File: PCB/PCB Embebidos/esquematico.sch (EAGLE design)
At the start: 27 parts, among them IC1 LM358N, IC2 317T, T1 BT138-V

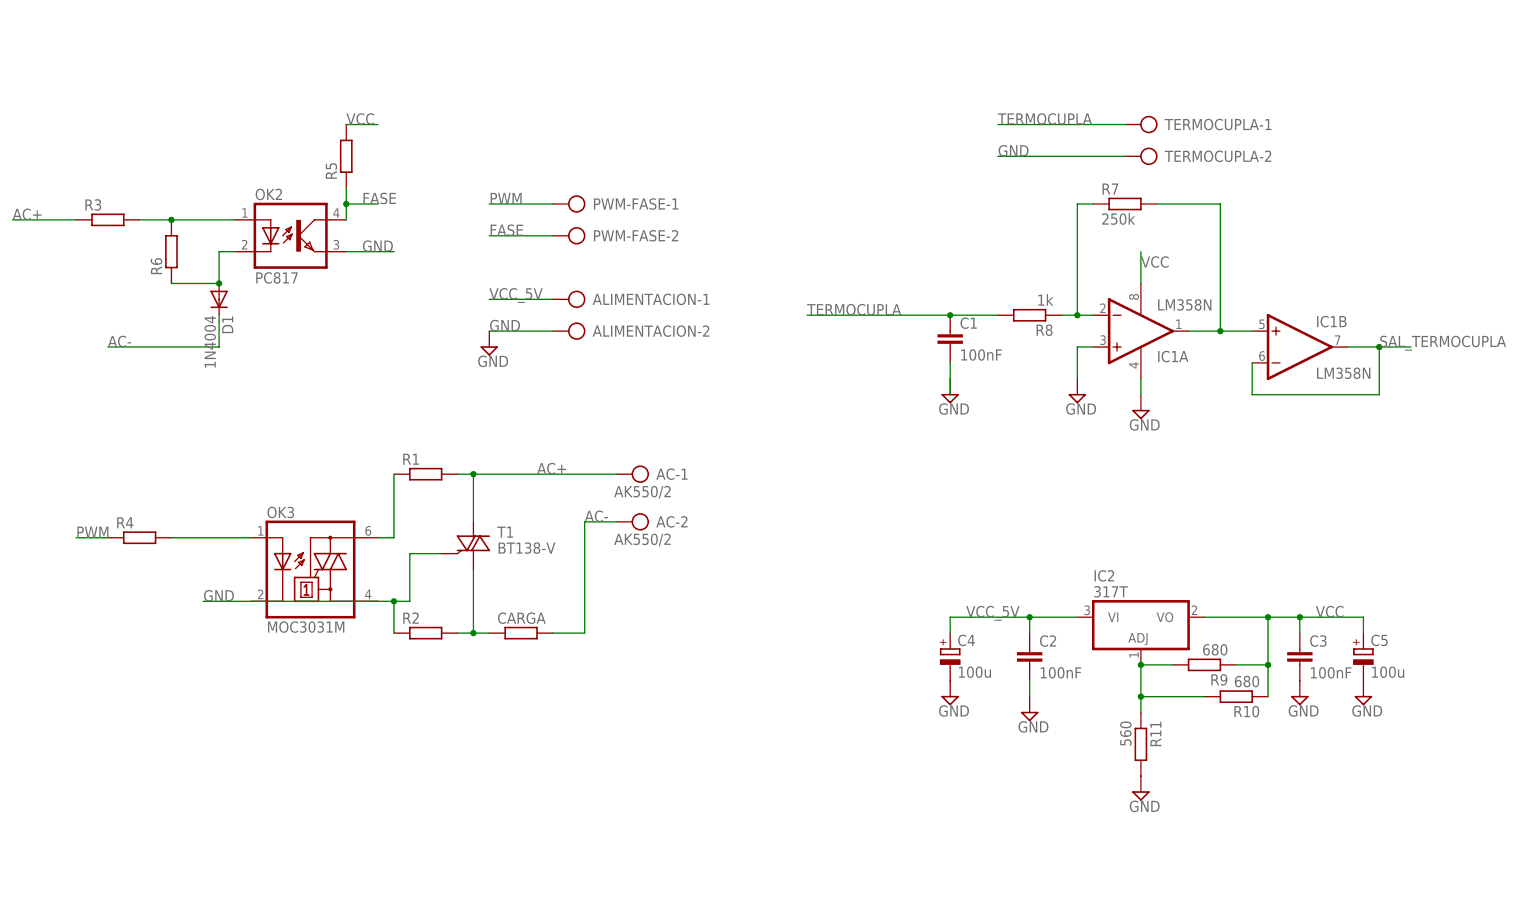
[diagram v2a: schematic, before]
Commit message: Cambie las resistencias del PCB a smd. Tambien modifique las borneras para usar unas de 5mm
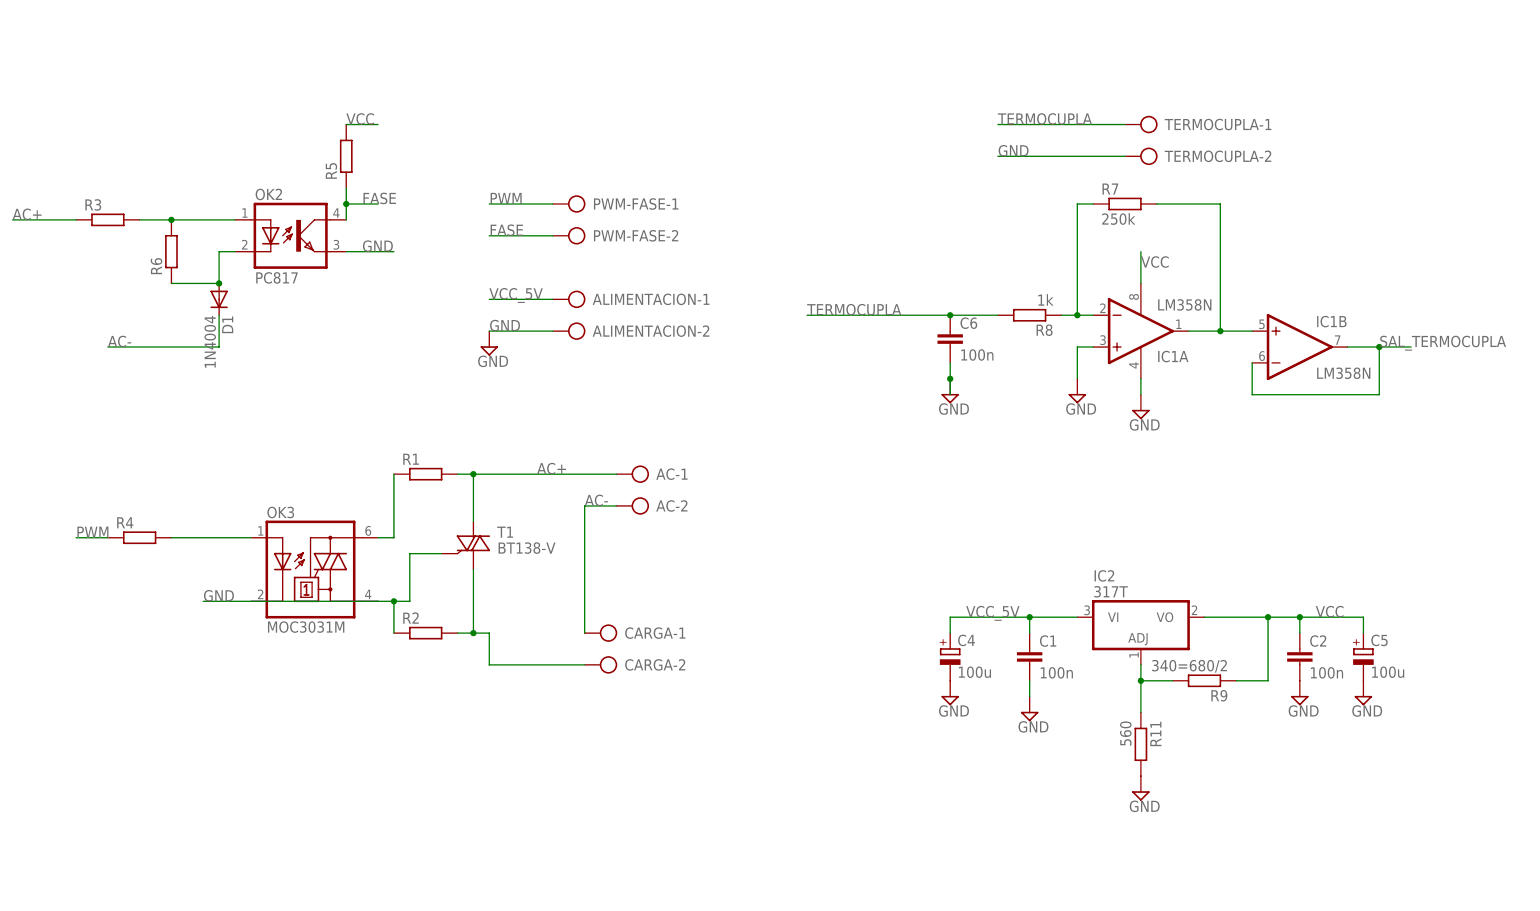
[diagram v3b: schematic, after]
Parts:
- removed C3: 100nF, capacitor-wima:C2,5-3
- removed R10: 680, resistor:R-EU_0207/10
- added C6: 100n, eagle-ltspice:CC1206
- AC: value AK550/2 -> (none); device con-ptr500:AK550/2 -> con-ptr500:AK300/2
- C1, C2: value 100nF -> 100n; device capacitor-wima:C2,5-3 -> eagle-ltspice:CC1206
- CARGA: device resistor:R-EU_0207/10 -> con-ptr500:AK300/2
- R1, R11, R2, R4, R5, R6, R7, R8: device resistor:R-EU_0207/10 -> resistor:R-EU_R1206
- R9: value 680 -> 340=680/2; device resistor:R-EU_0207/10 -> resistor:R-EU_R1206
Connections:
- net AC-: now also CARGA-1.KL; no longer AC-2.KL, CARGA.2
- net GND: now also C6.2; no longer C3.2
- net N$4: now also CARGA-2.KL; no longer CARGA.1
- net N$6: no longer R10.2
- net TERMOCUPLA: now also C6.1; no longer C1.1
- net VCC: now also C2.1; no longer C3.1, R10.1
- net VCC_5V: now also C1.1; no longer C2.1
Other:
- moved on the sheet: AC-2, C1, C2, R9

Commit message: Agregue los valores de algunas resistencias que me faltaban, agregue el pt100, y agregue un pdf con una foto del esquematico para poder revisarlo mas facil sin abrir eagle
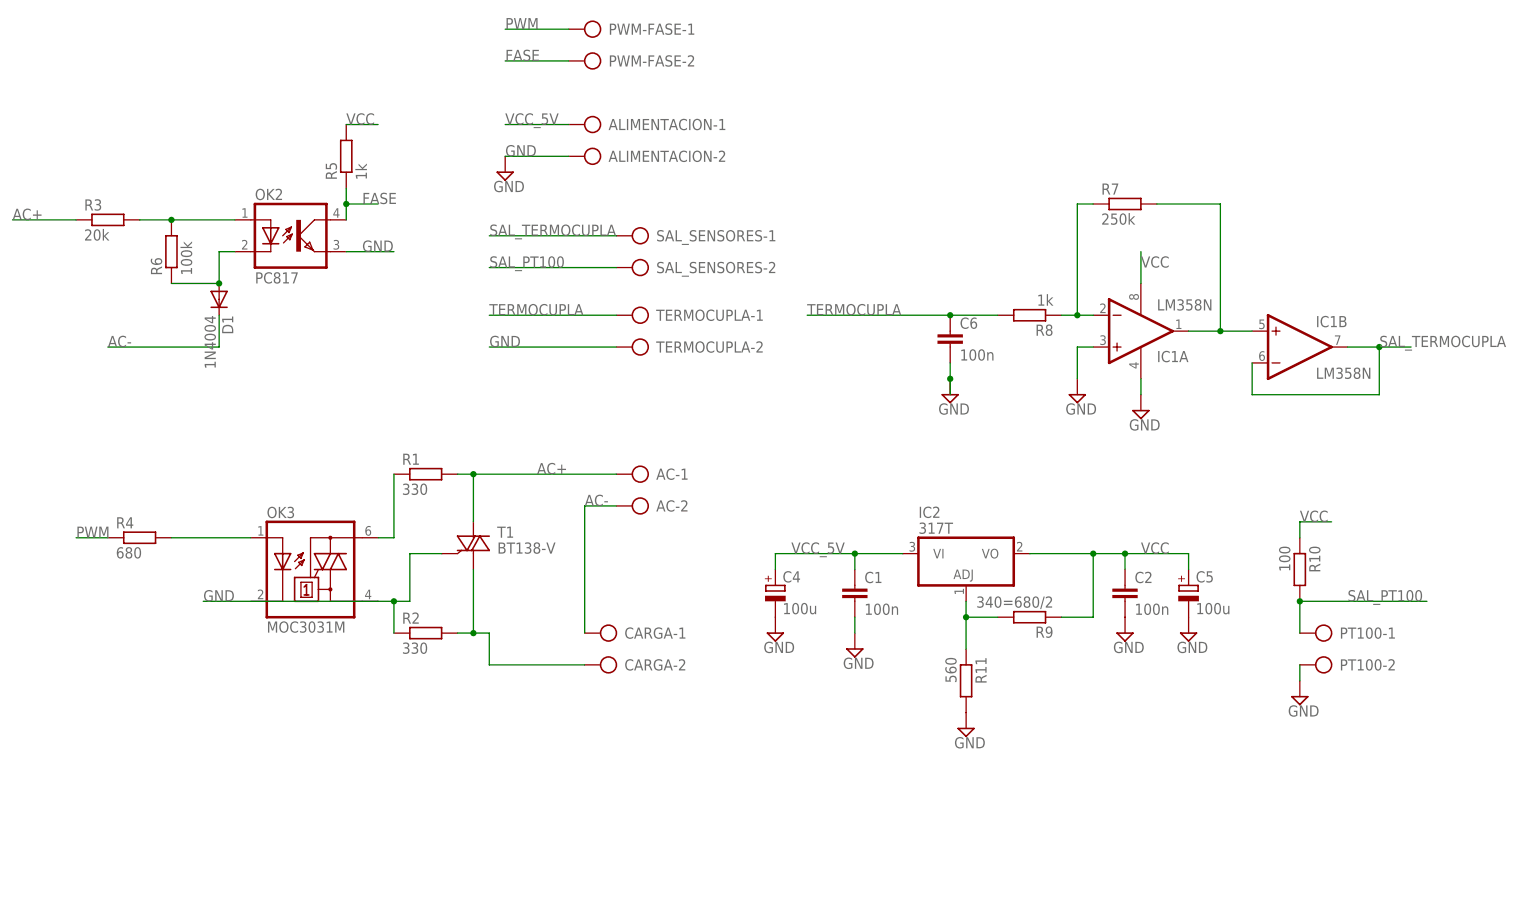
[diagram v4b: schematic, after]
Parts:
- added PT100, SAL_SENSORES: (no value), con-ptr500:AK300/2
- added R10: 100, resistor:R-EU_R1206
- R1, R2: value (none) -> 330
- R3: value (none) -> 20k
- R4: value (none) -> 680
- R5: value (none) -> 1k
- R6: value (none) -> 100k
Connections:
- new net SAL_PT100: PT100-1.KL, R10.2, SAL_SENSORES-2.KL
- net GND: now also PT100-2.KL
- net SAL_TERMOCUPLA: now also SAL_SENSORES-1.KL
- net VCC: now also R10.1
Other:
- moved on the sheet: ALIMENTACION-1, ALIMENTACION-2, C1, C2, C4, C5, IC2, PWM-FASE-1, PWM-FASE-2, R11, R9, TERMOCUPLA-1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

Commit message: Estuve presentando los componentes en la placa para ver mas o menos como va a quedar
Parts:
- added C3: 100n, eagle-ltspice:CC1206
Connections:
- net N$5: now also C3.1
- net N$7: now also C3.2
- net VCC: now also ALIMENTACION-1.KL
- net VCC_5V: no longer ALIMENTACION-1.KL
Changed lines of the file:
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@@
 <layer number="48" name="Document" color="7" fill="1" visible="yes" active="no"/>
 <layer number="49" name="Reference" color="7" fill="1" visible="yes" active="no"/>
-<layer number="51" name="tDocu" color="6" fill="1" visible="yes" active="no"/>
+<layer number="51" name="tDocu" color="7" fill="1" visible="yes" active="no"/>
 <layer number="52" name="bDocu" color="7" fill="1" visible="yes" active="no"/>
 <layer number="90" name="Modules" color="5" fill="1" visible="yes" active="yes"/>
@@
 <part name="SUPPLY10" library="supply2" deviceset="GND" device=""/>
 <part name="SAL_SENSORES" library="con-ptr500" deviceset="AK300/2" device=""/>
+<part name="C3" library="eagle-ltspice" deviceset="C" device="C1206" value="100n"/>
 </parts>
 <sheets>
@@
 <instance part="SAL_SENSORES" gate="-1" x="119.38" y="106.68" rot="MR0"/>
 <instance part="SAL_SENSORES" gate="-2" x="119.38" y="101.6" rot="MR0"/>
+<instance part="C3" gate="G$1" x="198.12" y="119.38" rot="R90"/>
 </instances>
 <busses>
@@
 <label x="223.52" y="60.96" size="1.778" layer="95"/>
 </segment>
+<segment>
+<wire x1="106.68" y1="124.46" x2="96.52" y2="124.46" width="0.1524" layer="91"/>
+<label x="96.52" y="124.46" size="1.778" layer="95"/>
+<pinref part="ALIMENTACION" gate="-1" pin="KL"/>
+</segment>
 </net>
 <net name="FASE" class="0">
@@
 <wire x1="187.96" y1="111.76" x2="187.96" y2="93.98" width="0.1524" layer="91"/>
 <junction x="187.96" y="93.98"/>
+<pinref part="C3" gate="G$1" pin="1"/>
+<wire x1="195.58" y1="119.38" x2="187.96" y2="119.38" width="0.1524" layer="91"/>
+<wire x1="187.96" y1="119.38" x2="187.96" y2="111.76" width="0.1524" layer="91"/>
+<junction x="187.96" y="111.76"/>
 </segment>
 </net>
@@
 <wire x1="215.9" y1="91.44" x2="210.82" y2="91.44" width="0.1524" layer="91"/>
 <junction x="210.82" y="91.44"/>
+<pinref part="C3" gate="G$1" pin="2"/>
+<wire x1="203.2" y1="119.38" x2="210.82" y2="119.38" width="0.1524" layer="91"/>
+<wire x1="210.82" y1="119.38" x2="210.82" y2="111.76" width="0.1524" layer="91"/>
+<junction x="210.82" y="111.76"/>
 </segment>
 </net>
@@
 <net name="VCC_5V" class="0">
 <segment>
-<wire x1="106.68" y1="124.46" x2="96.52" y2="124.46" width="0.1524" layer="91"/>
-<label x="96.52" y="124.46" size="1.778" layer="95"/>
-<pinref part="ALIMENTACION" gate="-1" pin="KL"/>
-</segment>
-<segment>
 <pinref part="IC2" gate="A1" pin="VI"/>

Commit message: Estuve ruteando el PCB. Creo que esta terminado, pero tendria que revisarlo menos dormido
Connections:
- net AC-: now also AC-2.KL, CARGA-2.KL; no longer CARGA-1.KL
- net GND: now also ALIMENTACION-1.KL, OK3.C; no longer ALIMENTACION-2.KL
- net N$4: now also CARGA-1.KL; no longer CARGA-2.KL
- net VCC: now also ALIMENTACION-2.KL; no longer ALIMENTACION-1.KL
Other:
- moved on the sheet: ALIMENTACION-1, ALIMENTACION-2, CARGA-1, CARGA-2
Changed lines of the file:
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@@
 <instance part="C1" gate="G$1" x="152.4" y="50.8"/>
 <instance part="C2" gate="G$1" x="195.58" y="50.8"/>
-<instance part="ALIMENTACION" gate="-1" x="111.76" y="124.46" rot="MR0"/>
-<instance part="ALIMENTACION" gate="-2" x="111.76" y="119.38" rot="MR0"/>
+<instance part="ALIMENTACION" gate="-1" x="111.76" y="119.38" rot="MR0"/>
+<instance part="ALIMENTACION" gate="-2" x="111.76" y="124.46" rot="MR0"/>
 <instance part="AC" gate="-1" x="119.38" y="68.58" rot="MR0"/>
 <instance part="AC" gate="-2" x="119.38" y="63.5" rot="MR0"/>
-<instance part="CARGA" gate="-1" x="114.3" y="43.18" rot="MR0"/>
-<instance part="CARGA" gate="-2" x="114.3" y="38.1" rot="MR0"/>
+<instance part="CARGA" gate="-1" x="114.3" y="38.1" rot="MR0"/>
+<instance part="CARGA" gate="-2" x="114.3" y="43.18" rot="MR0"/>
 <instance part="R10" gate="G$1" x="223.52" y="53.34" rot="R270"/>
 <instance part="PT100" gate="-1" x="228.6" y="43.18" rot="MR0"/>
@@
 <junction x="91.44" y="43.18"/>
 <wire x1="93.98" y1="38.1" x2="93.98" y2="43.18" width="0.1524" layer="91"/>
-<pinref part="CARGA" gate="-2" pin="KL"/>
+<pinref part="CARGA" gate="-1" pin="KL"/>
 <wire x1="109.22" y1="38.1" x2="93.98" y2="38.1" width="0.1524" layer="91"/>
 </segment>
@@
 <net name="GND" class="0">
 <segment>
-<wire x1="106.68" y1="119.38" x2="96.52" y2="119.38" width="0.1524" layer="91"/>
-<label x="96.52" y="119.38" size="1.778" layer="95"/>
-<pinref part="SUPPLY1" gate="GND" pin="GND"/>
-<pinref part="ALIMENTACION" gate="-2" pin="KL"/>
-</segment>
-<segment>
 <pinref part="OK2" gate="A" pin="EMIT"/>
 <wire x1="71.12" y1="104.14" x2="78.74" y2="104.14" width="0.1524" layer="91"/>
 <label x="73.66" y="104.14" size="1.778" layer="95"/>
-</segment>
-<segment>
-<wire x1="48.26" y1="48.26" x2="76.2" y2="48.26" width="0.1524" layer="91"/>
-<label x="48.26" y="48.26" size="1.778" layer="95"/>
 </segment>
 <segment>
@@
 <wire x1="223.52" y1="38.1" x2="223.52" y2="35.56" width="0.1524" layer="91"/>
 </segment>
+<segment>
+<pinref part="OK3" gate="-1" pin="C"/>
+<wire x1="55.88" y1="48.26" x2="35.56" y2="48.26" width="0.1524" layer="91"/>
+<label x="35.56" y="48.26" size="1.778" layer="95"/>
+</segment>
+<segment>
+<pinref part="ALIMENTACION" gate="-1" pin="KL"/>
+<pinref part="SUPPLY1" gate="GND" pin="GND"/>
+<wire x1="106.68" y1="119.38" x2="96.52" y2="119.38" width="0.1524" layer="91"/>
+<label x="96.52" y="119.38" size="1.778" layer="95"/>
+</segment>
 </net>
 <net name="PWM" class="0">
@@
 <net name="AC-" class="0">
 <segment>
+<label x="109.22" y="63.5" size="1.778" layer="95"/>
+<pinref part="AC" gate="-2" pin="KL"/>
+<wire x1="114.3" y1="63.5" x2="109.22" y2="63.5" width="0.1524" layer="91"/>
+<pinref part="CARGA" gate="-2" pin="KL"/>
 <wire x1="109.22" y1="43.18" x2="109.22" y2="63.5" width="0.1524" layer="91"/>
-<wire x1="109.22" y1="63.5" x2="114.3" y2="63.5" width="0.1524" layer="91"/>
-<label x="109.22" y="63.5" size="1.778" layer="95"/>
-<pinref part="CARGA" gate="-1" pin="KL"/>
 </segment>
 <segment>
@@
 </segment>
 <segment>
+<pinref part="ALIMENTACION" gate="-2" pin="KL"/>
 <wire x1="106.68" y1="124.46" x2="96.52" y2="124.46" width="0.1524" layer="91"/>
 <label x="96.52" y="124.46" size="1.778" layer="95"/>
-<pinref part="ALIMENTACION" gate="-1" pin="KL"/>
-</segment>
-</net>
+</segment>
+</net>
